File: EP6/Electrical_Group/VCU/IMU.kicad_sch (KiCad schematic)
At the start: 8 parts, among them J20 I2C, U12 LSM6DSOX

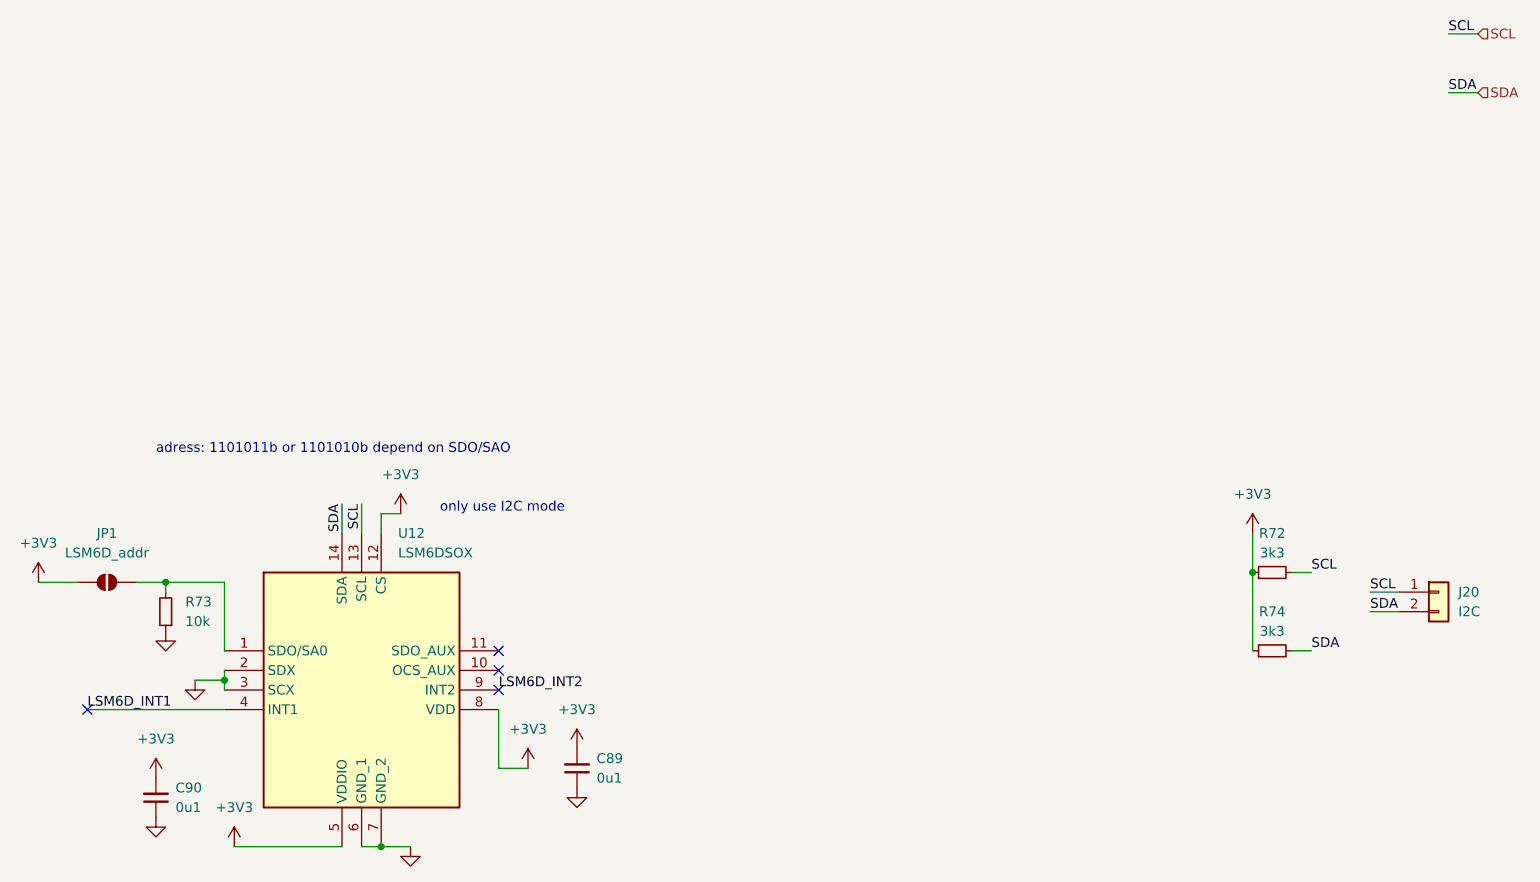
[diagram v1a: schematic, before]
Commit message: udpate VCU to V3.0
V3.0 move mounting point out a little
     remove HSUSB
     remove brake light
     change conn pinout to match dashboard V1.0
     add CAN2
     add some LEDs
     Etc.
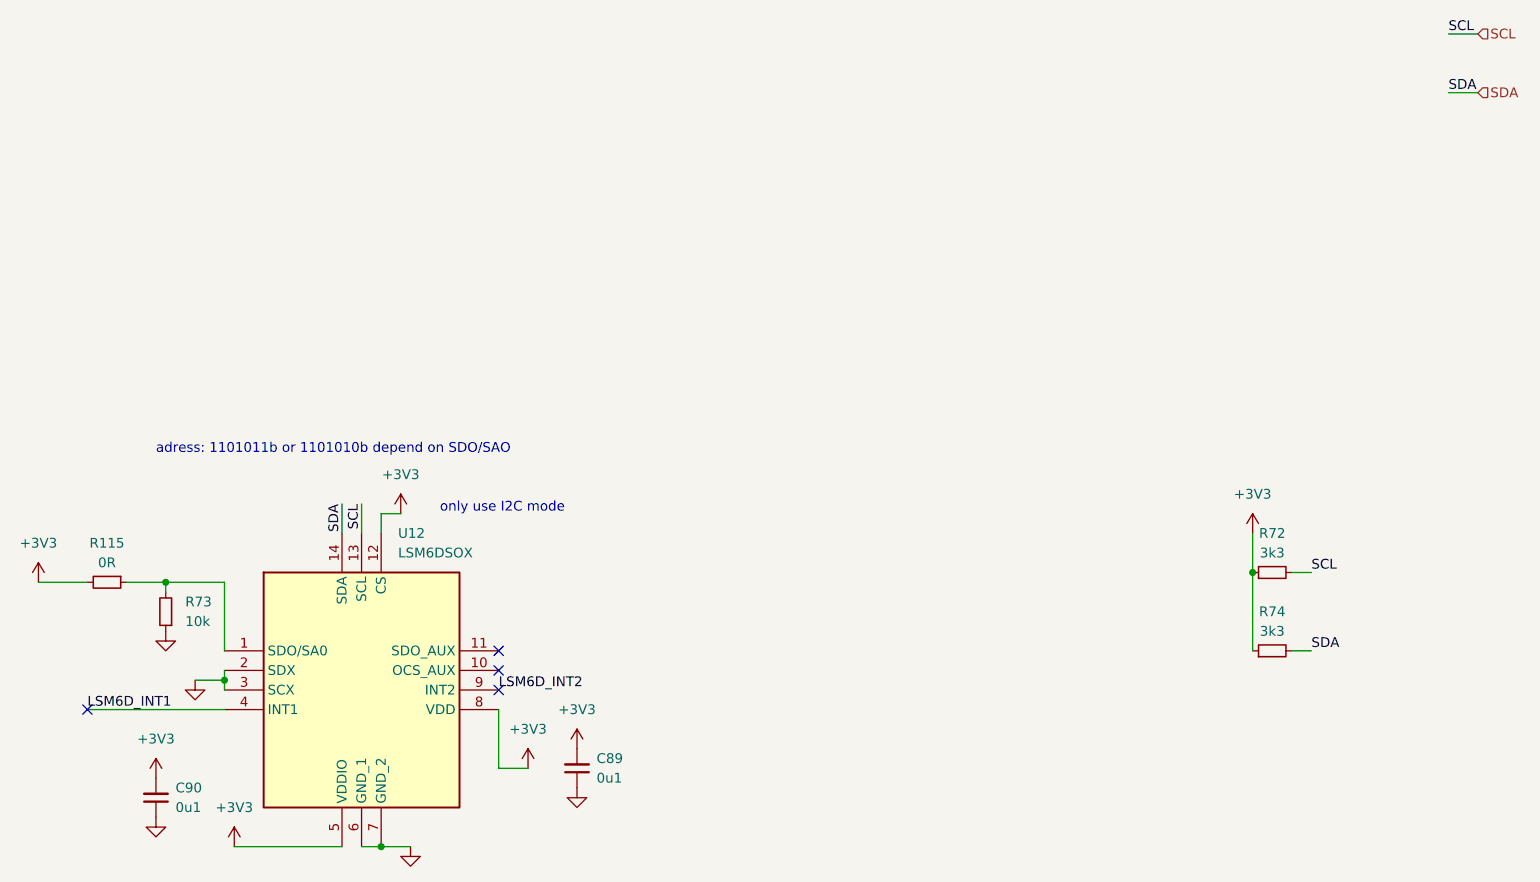
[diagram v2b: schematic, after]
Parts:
- removed J20: I2C, Connector_PinHeader_2.54mm:PinHeader_1x02_P2.54mm_Vertical, symbol Connector_Generic:Conn_01x02
- removed JP1: LSM6D_addr, Jumper:SolderJumper-2_P1.3mm_Open_RoundedPad1.0x1.5mm, symbol Jumper:SolderJumper_2_Open
- added R115: 0R, Resistor_SMD:R_0402_1005Metric, symbol Device:R_Small
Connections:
- net +3V3: now also R115.2
- net at R73.2, U12.1 (SDO/SA0): now also R115.1
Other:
- title: EP6 VCU -> VCU
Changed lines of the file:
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@@
 	(generator "eeschema")
 	(generator_version "8.0")
-	(paper "A4")
+	(paper "A3")
 	(title_block
-		(title "EP6 VCU")
-		(date "2024-12-05")
-		(rev "2.0")
+		(title "VCU")
+		(date "2025-06-29")
+		(rev "3.0")
 		(company "NTURacing")
-		(comment 1 "Jerrymk, ML Tsou, 郭哲明 Jack Kuo")
+		(comment 1 " 郭哲明 Jack Kuo, Jerrymk, ML Tsou")
 		(comment 2 "Electrical group")
 	)
@@
 	(wire
 		(pts
-			(xy 59.69 109.22) (xy 63.5 109.22)
+			(xy 58.42 109.22) (xy 63.5 109.22)
 		)
 		(stroke
@@
 	(wire
 		(pts
-			(xy 219.71 110.49) (xy 223.52 110.49)
-		)
-		(stroke
-			(width 0)
-			(type default)
-		)
-	)
-	(wire
-		(pts
 			(xy 63.5 110.49) (xy 63.5 109.22)
 		)
@@
 	(wire
 		(pts
-			(xy 219.71 113.03) (xy 223.52 113.03)
-		)
-		(stroke
-			(width 0)
-			(type default)
-		)
-	)
-	(wire
-		(pts
 			(xy 86.36 99.06) (xy 86.36 102.87)
 		)
@@
 	(wire
 		(pts
-			(xy 46.99 109.22) (xy 52.07 109.22)
+			(xy 46.99 109.22) (xy 53.34 109.22)
 		)
 		(stroke
@@
 		)
 	)
-	(label "SCL"
-		(at 219.71 110.49 0)
-		(effects
-			(font
-				(size 1.27 1.27)
-			)
-			(justify left bottom)
-		)
-	)
 	(label "SDA"
 		(at 229.87 45.72 0)
@@
 	(label "LSM6D_INT2"
 		(at 106.68 123.19 0)
-		(effects
-			(font
-				(size 1.27 1.27)
-			)
-			(justify left bottom)
-		)
-	)
-	(label "SDA"
-		(at 219.71 113.03 0)
 		(effects
 			(font
@@
 	)
 	(symbol
-		(lib_id "Jumper:SolderJumper_2_Open")
-		(at 55.88 109.22 0)
-		(unit 1)
-		(exclude_from_sim no)
-		(in_bom yes)
-		(on_board yes)
-		(dnp no)
-		(fields_autoplaced yes)
-		(property "Reference" "JP1"
-			(at 55.88 102.87 0)
-			(effects
-				(font
-					(size 1.27 1.27)
-				)
-			)
-		)
-		(property "Value" "LSM6D_addr"
-			(at 55.88 105.41 0)
-			(effects
-				(font
-					(size 1.27 1.27)
-				)
-			)
-		)
-		(property "Footprint" "Jumper:SolderJumper-2_P1.3mm_Open_RoundedPad1.0x1.5mm"
-			(at 55.88 109.22 0)
-			(effects
-				(font
-					(size 1.27 1.27)
-				)
-				(hide yes)
-			)
-		)
-		(property "Datasheet" "~"
-			(at 55.88 109.22 0)
-			(effects
-				(font
-					(size 1.27 1.27)
-				)
-				(hide yes)
-			)
-		)
-		(property "Description" "Solder Jumper, 2-pole, open"
-			(at 55.88 109.22 0)
-			(effects
-				(font
-					(size 1.27 1.27)
-				)
-				(hide yes)
-			)
-		)
-		(pin "1"
-		)
-		(pin "2"
-		)
-		(instances
-			(project "power board"
-				(path "/eb296f24-894e-4ea0-b0cd-3ba211155378/6b07e066-83b3-4447-a68e-5f9edbcb1e93"
-					(reference "JP1")
-					(unit 1)
-				)
-			)
-		)
-	)
-	(symbol
 		(lib_id "power:+3V3")
 		(at 204.47 102.87 0)
@@
 	)
 	(symbol
+		(lib_id "Device:R_Small")
+		(at 55.88 109.22 270)
+		(unit 1)
+		(exclude_from_sim no)
+		(in_bom yes)
+		(on_board yes)
+		(dnp no)
+		(fields_autoplaced yes)
+		(property "Reference" "R115"
+			(at 55.88 104.14 90)
+			(effects
+				(font
+					(size 1.27 1.27)
+				)
+			)
+		)
+		(property "Value" "0R"
+			(at 55.88 106.68 90)
+			(effects
+				(font
+					(size 1.27 1.27)
+				)
+			)
+		)
+		(property "Footprint" "Resistor_SMD:R_0402_1005Metric"
+			(at 55.88 109.22 0)
+			(effects
+				(font
+					(size 1.27 1.27)
+				)
+				(hide yes)
+			)
+		)
+		(property "Datasheet" "~"
+			(at 55.88 109.22 0)
+			(effects
+				(font
+					(size 1.27 1.27)
+				)
+				(hide yes)
+			)
+		)
+		(property "Description" "Resistor, small symbol"
+			(at 55.88 109.22 0)
+			(effects
+				(font
+					(size 1.27 1.27)
+				)
+				(hide yes)
+			)
+		)
+		(pin "1"
+		)
+		(pin "2"
+		)
+		(instances
+			(project "VCU"
+				(path "/eb296f24-894e-4ea0-b0cd-3ba211155378/6b07e066-83b3-4447-a68e-5f9edbcb1e93"
+					(reference "R115")
+					(unit 1)
+				)
+			)
+		)
+	)
+	(symbol
 		(lib_id "power:GND")
 		(at 63.5 115.57 0)
@@
 					(unit 1)
 				)
-			)
-		)
-	)
-	(symbol
-		(lib_id "Connector_Generic:Conn_01x02")
-		(at 228.6 110.49 0)
-		(unit 1)
-		(exclude_from_sim no)
-		(in_bom yes)
-		(on_board yes)
-		(dnp no)
-		(property "Reference" "J20"
-			(at 231.14 110.49 0)
-			(effects
-				(font
-					(size 1.27 1.27)
-				)
-				(justify left)
-			)
-		)
-		(property "Value" "I2C"
-			(at 231.14 113.03 0)
-			(effects
-				(font
-					(size 1.27 1.27)
-				)
-				(justify left)
-			)
-		)
-		(property "Footprint" "Connector_PinHeader_2.54mm:PinHeader_1x02_P2.54mm_Vertical"
-			(at 228.6 110.49 0)
-			(effects
-				(font
-					(size 1.27 1.27)
-				)
-				(hide yes)
-			)
-		)
-		(property "Datasheet" "~"
-			(at 228.6 110.49 0)
-			(effects
-				(font
-					(size 1.27 1.27)
-				)
-				(hide yes)
-			)
-		)
-		(property "Description" "Generic connector, single row, 01x02, script generated (kicad-library-utils/schlib/autogen/connector/)"
-			(at 228.6 110.49 0)
-			(effects
-				(font
-					(size 1.27 1.27)
-				)
-				(hide yes)
-			)
-		)
-		(pin "1"
-		)
-		(pin "2"
-		)
-		(instances
-			(project "power board"
-				(path "/eb296f24-894e-4ea0-b0cd-3ba211155378/6b07e066-83b3-4447-a68e-5f9edbcb1e93"
-					(reference "J20")
-					(unit 1)
-				)
